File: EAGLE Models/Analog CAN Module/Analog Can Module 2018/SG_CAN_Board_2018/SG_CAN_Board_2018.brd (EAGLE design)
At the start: 89.9 x 38 mm, 106 parts, among them IC1 AT90CAN128, IC2 MCP2551SO8, IC3 NUP2105L, IC5 FT232RL, Q1 56P2859, U1 LTC2053, U11 LTC2053, U12 LTC2053, U2 LTC2053, U3 LTC2053, U4 LTC2053

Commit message: CAN Boards Finished
Passes DFM!
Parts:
- removed D2: 1N5819, diode:DO41-7.6
- added U$4: 1N5819, diode:1N5819SM
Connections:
- net 12V: now also U$4.P$1; no longer D2.A
- net 5V_REG_IN: now also U$4.P$2; no longer D2.C
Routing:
- net TCO1: track 71.9 -> 52.1 mm
- net DGND: track 244.4 -> 229.9 mm, vias 8 -> 9
- net AGND: track 348.8 -> 355.2 mm, vias 21 -> 20
- net 12V: track 47.5 -> 44.7 mm
- net 2V5REF: track 96.2 -> 98.3 mm
- net 5V_REG_IN: track 7.50 -> 6.06 mm
- net N$5: track 13.5 -> 14.9 mm
- net RESET: track 34.0 -> 32.6 mm
- net N$12: track 12.9 -> 14.3 mm
- net N$7: track 20.4 -> 21.7 mm
- net SG5V: track 66.4 -> 65.2 mm
- net VCC: track 324.4 -> 325.4 mm
- net RX: track 21.7 -> 22.6 mm

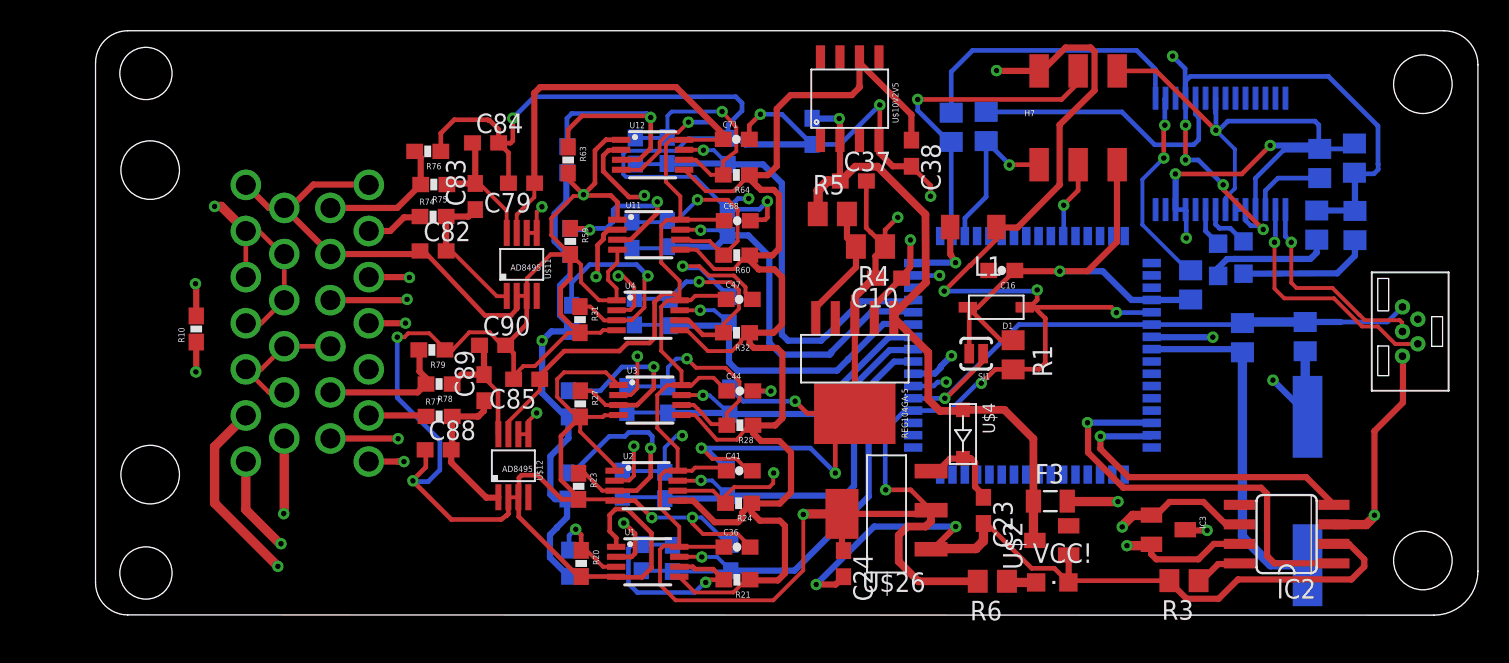
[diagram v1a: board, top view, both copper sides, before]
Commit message: SG CAN Board Changes
-85% done with requested changes
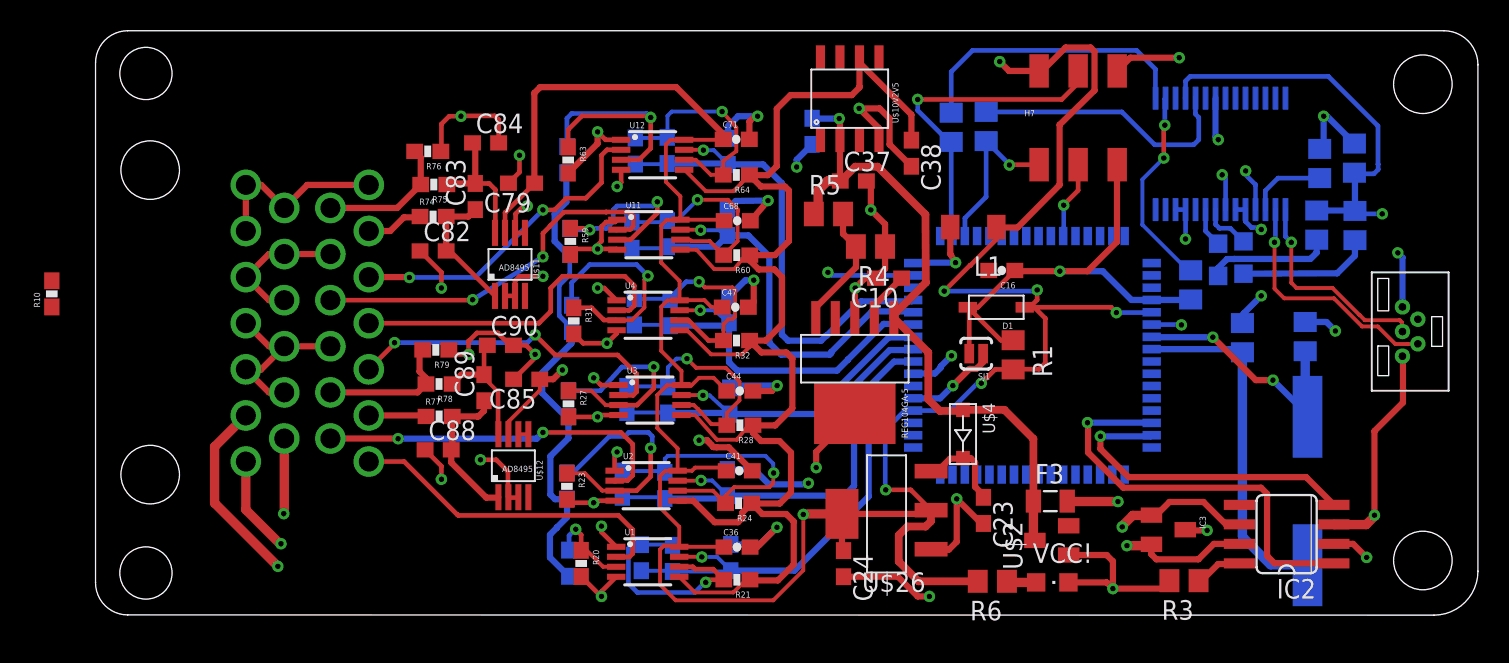
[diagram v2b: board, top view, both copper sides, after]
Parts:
- moved R10 9.67 mm to (-2.74, 21.0)
- moved R23 0.76 mm to (30.8, 8.43)
- moved R27 0.76 mm to (30.9, 13.8)
- moved U$11 0.76 mm to (27.1, 22.9)
- moved C47 0.57 mm to (41.7, 20.1)
- moved C90 0.51 mm to (26.4, 17.6)
- moved R32 0.51 mm to (41.8, 17.9)
- moved R31 0.41 mm to (31.2, 19.2)
- moved R5 0.25 mm to (47.8, 26.2)
- moved R79 0.25 mm to (22.2, 17.3)
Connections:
- net AGND: now also U$3.B11, U$3.B17, U$3.B18, U$3.B23, U$3.B24; no longer U$3.B1, U$3.B14, U$3.B20, U$3.B9
- net DGND: now also U$3.B1, U$3.B14, U$3.B20, U$3.B21; no longer U$3.B11, U$3.B17, U$3.B18, U$3.B24
- net VCC: now also U$3.B9; no longer U$3.B21, U$3.B23
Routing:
- net AGND: track 355.2 -> 146.5 mm, vias 20 -> 32
- net DGND: track 229.9 -> 77.6 mm, vias 9 -> 16
- net TCO1: track 52.1 -> 5.92 mm
- net VCC: track 325.4 -> 283.5 mm, vias 14 -> 11
- net TCO2: track 32.0 -> 0.65 mm, vias 2 -> 0
- net SG5V: track 65.2 -> 35.1 mm, vias 2 -> 0
- net SG_6: track 27.6 -> 20.9 mm
- net SG_5: track 22.0 -> 24.6 mm
- net 2V5REF: track 98.3 -> 100.1 mm
- net N$7: track 21.7 -> 20.1 mm, vias 2 -> 1
- net SG_4: track 21.3 -> 22.3 mm, vias 2 -> 0
- net N$8: track 13.3 -> 14.0 mm
- net N$5: track 14.9 -> 15.7 mm
- net SG_3: track 21.4 -> 21.9 mm, vias 1 -> 2
- net SG_1: track 21.9 -> 21.7 mm, vias 2 -> 0

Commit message: SG CAN Board Update
-100% done routing, passed DRC
-waiting review, will check DFM after
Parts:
- moved R10 24.9 mm to (19.2, 32.7), turned to 0 degrees
- moved R60 0.25 mm to (41.8, 23.7)
- moved C68 0.25 mm to (41.9, 26.0)
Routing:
- net VCC: track 283.5 -> 159.1 mm, vias 11 -> 16
- net SG5V: track 35.1 -> 73.4 mm, vias 0 -> 1
- net TCO2: track 0.65 -> 33.7 mm, vias 0 -> 3
- net TCO1: track 5.92 -> 38.5 mm, vias 2 -> 4
- net AGND: track 146.5 -> 159.6 mm, vias 32 -> 33
- net DGND: track 77.6 -> 87.5 mm, vias 16 -> 18
- net N$12: track 14.7 -> 12.1 mm
- net 2V5REF: track 100.1 -> 102.6 mm, vias 0 -> 2
- net 12V: track 44.9 -> 45.7 mm
- net N$14: track 14.5 -> 13.8 mm
- net N$5: track 15.7 -> 15.1 mm

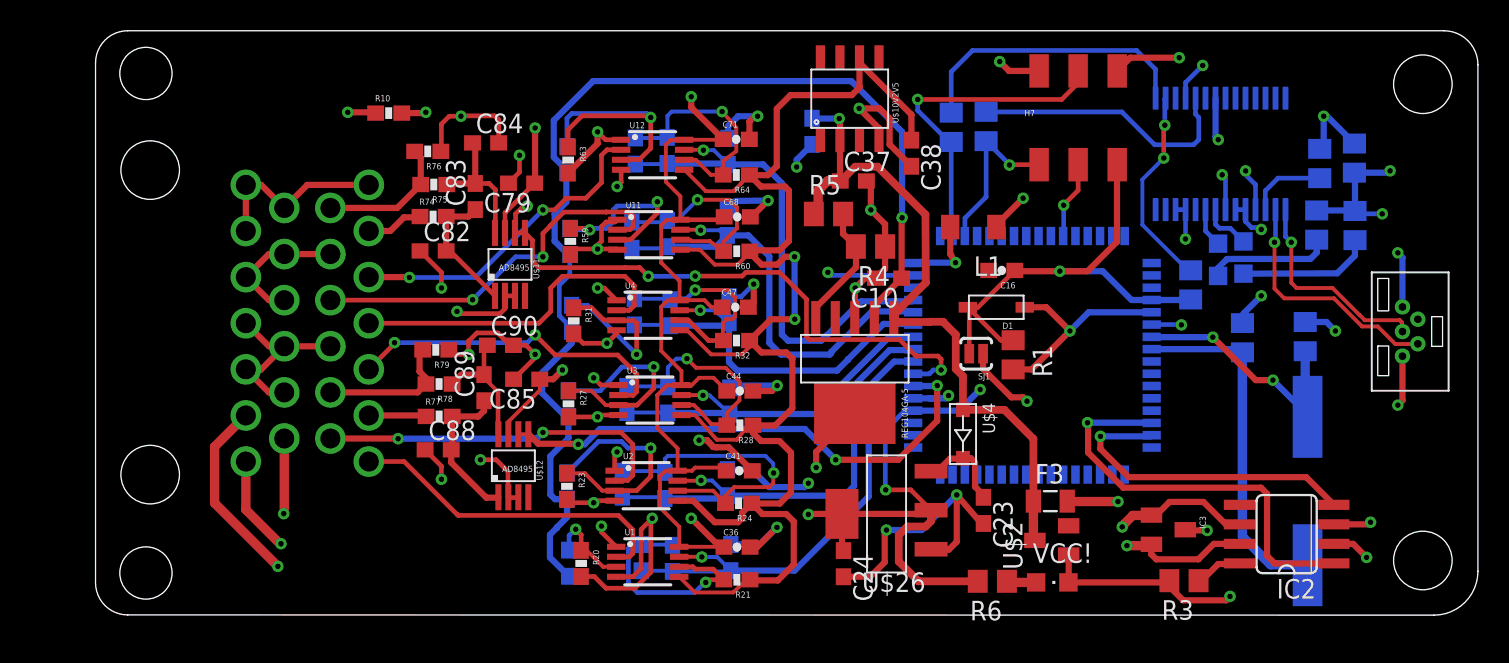
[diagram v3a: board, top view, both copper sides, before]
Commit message: SG CAN Board Update
- fixed crystal orientation, ground planes,  VCC power to SG op amps, CAN lines
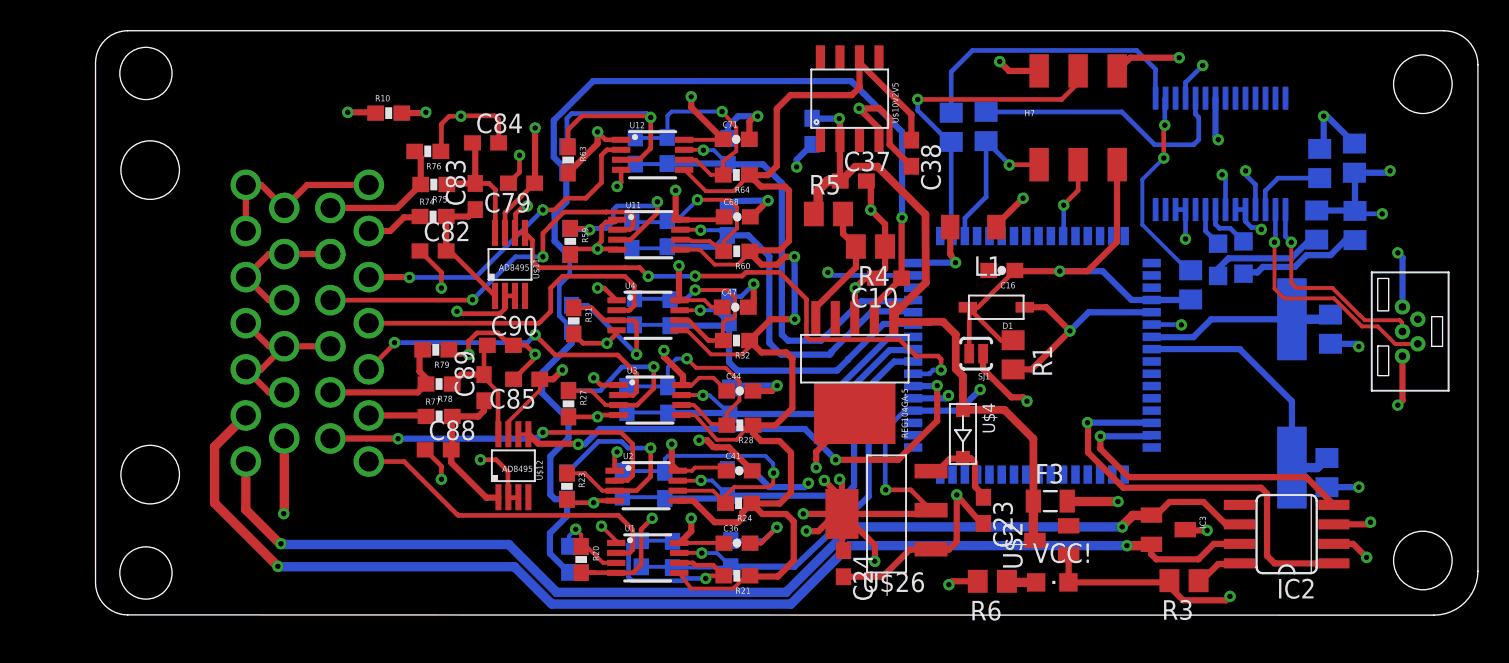
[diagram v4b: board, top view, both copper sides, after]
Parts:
- moved C1 10.4 mm to (80.2, 9.33), turned to 90 degrees
- moved Q1 6.43 mm to (77.9, 14.5)
- moved C2 1.71 mm to (80.4, 18.7), turned to 90 degrees
- moved C36 0.25 mm to (41.8, 4.73)
- moved C39 0.25 mm to (41.4, 4.05)
- moved R22 0.25 mm to (35.6, 4.05)
- moved C35 0.25 mm to (37.6, 4.00)
- moved R18 0.25 mm to (30.9, 3.68)
- moved R20 0.25 mm to (31.7, 3.67)
- moved R21 0.25 mm to (41.8, 2.61)
- moved U1 0.25 mm to (36.0, 3.78)
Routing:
- net VCC: track 159.1 -> 136.6 mm, vias 16 -> 25
- net AGND: track 159.6 -> 153.0 mm
- net XTAL1: track 17.9 -> 12.2 mm, vias 2 -> 0
- net DGND: track 87.5 -> 81.9 mm, vias 18 -> 17
- net N$11: track 23.0 -> 18.7 mm
- net CAN_L: track 70.6 -> 73.3 mm
- net CAN_H: track 76.9 -> 78.8 mm
- net N$36: track 8.74 -> 8.16 mm
- net N$35: track 8.19 -> 7.67 mm

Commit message: SG CAN Board Updates/Reference designators
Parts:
- renumbered H7 to J7, U$1 to J1, U$10V2V5 to IC4, U$11 to IC15, U$12 to IC16, U$2 to D2, U$26 to IC6, U$3 to J2, U$4 to D4, U$5 to IC7, U1 to IC8, U11 to IC12, U12 to IC13, U2 to IC9, U3 to IC10, U4 to IC11, VCC! to LED4
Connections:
- net AGND: no longer J2.B23
- net VCC: now also J2.B23
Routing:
- net AGND: track 153.0 -> 149.5 mm
- net VCC: track 136.6 -> 139.8 mm
- net DGND: track 81.9 -> 81.5 mm, vias 17 -> 18
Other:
- board text removed: "C:/Users/Aiku/Downloads/CPRacingSLO-BW-Final(1).bmp"
